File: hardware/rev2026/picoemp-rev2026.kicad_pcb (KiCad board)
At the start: 2 copper layers, 40 x 130 mm, 53 parts, among them J1 EDGE-SMA, J2 1x2_Pin_Header, J3 MKDS 1,5/2-5.08, J4 EDGE-SMA, P1 Header 7, P2 Header 2, P3 Header 4, Q1 LDA111STR, Q2 RGT16BM65DTL, Q3 AO3422, Q4 AO3422, SW1 KSC741J LFS, SW2 KSC741J LFS, SW3 TL3301AF160QJ, T1 ATB322524, T2 ATB322524, U1 SC0915, U2 74LVC1G17

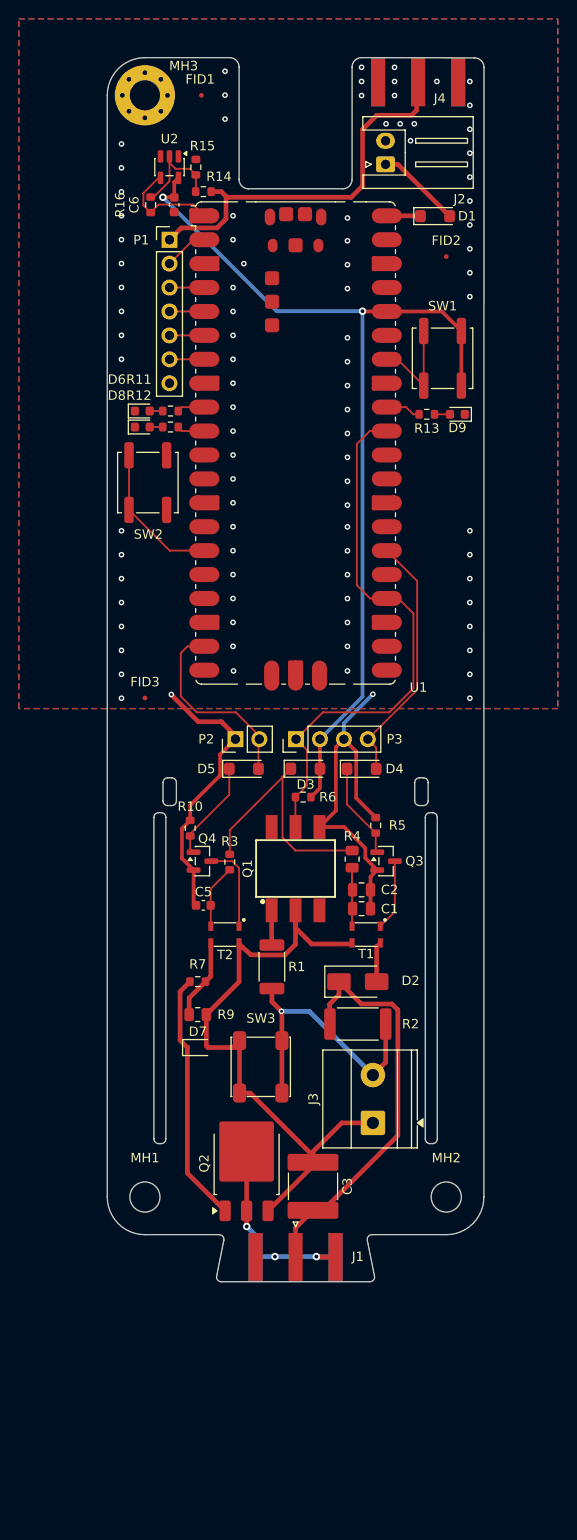
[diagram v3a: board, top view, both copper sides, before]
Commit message: Checkpoint: board origin shift, HV warning marks, intra-HV rule
Committing work that had been sitting uncommitted in the working tree, so the
1551G shield changes can be replayed on top of it without risking it.

  - whole board translated +25.400 mm in Y (X unchanged); origin was 19.872,
    now 45.272
  - two Symbol_HighVoltage_NoTriangle_2x5mm_Copper marks added at the board
    edges beside the HV section, (106.900,139.300) and (141.900,139.300),
    both carrying the unannotated reference REF**
  - .dru gains "Intra-HV spacing at full rail voltage": 0.8 mm, warning
    severity, scoped to the three pairs that genuinely stand at the rail --
    HV_RTN against HV_SENSE, HV_RAIL and HV_OUT. The barrier rule is
    HV-to-non-HV and says nothing about these.
  - schematic: 3 wires, 3 junctions and some repositioning; no component,
    value or property changes
  - LAYOUT-HANDOFF.md rewritten from instructions into a record

Gates at this commit: 66 tests pass; DRC with errors and warnings reports 0
violations, 0 unconnected, 0 footprint errors, exit 0. The new rule fires
correctly and finds nothing -- the header comment claiming 9 violations
predates the fixes that cleared them.

Co-Authored-By: Claude Opus 5 <noreply@anthropic.com>
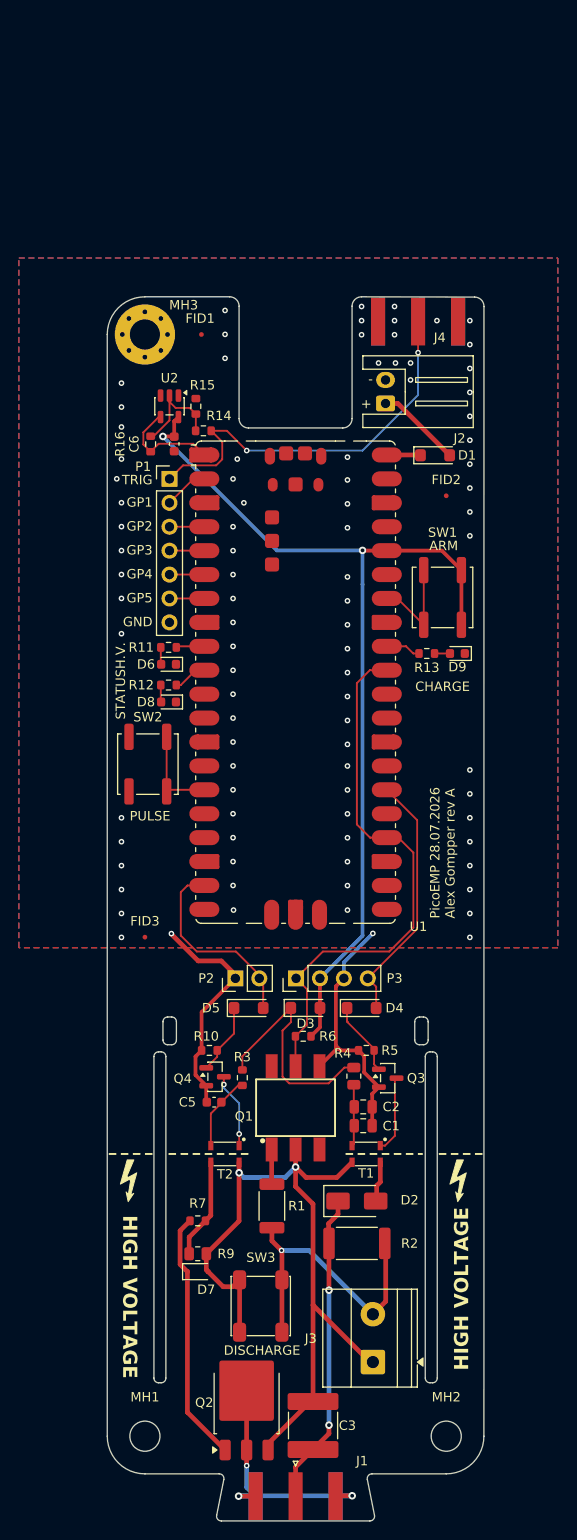
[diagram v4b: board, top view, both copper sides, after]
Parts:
- added REF**: Symbol_HighVoltage_NoTriangle_2x5mm_Copper, Symbol:Symbol_HighVoltage_NoTriangle_2x5mm_Copper, F.Cu at (106.9, 139.3)
- added REF**: Symbol_HighVoltage_NoTriangle_2x5mm_Copper, Symbol:Symbol_HighVoltage_NoTriangle_2x5mm_Copper, F.Cu at (141.9, 139.3)
- moved SW2 29.9 mm to (108.7, 94.9), turned to -90 degrees
- moved D8 29.3 mm to (110.9, 88.3), turned to 180 degrees
- moved R12 27.4 mm to (110.9, 86.5)
- moved D6 27.0 mm to (110.9, 84.3), turned to 180 degrees
- moved D5 25.4 mm to (119.4, 120.8)
- moved D3 25.4 mm to (125.4, 120.8)
- moved D9 25.4 mm to (141.6, 83.2)
- moved FID2 25.4 mm to (140.4, 66.4)
- moved FID3 25.4 mm to (108.4, 113.3)
- moved J3 25.4 mm to (132.6, 158.4)
- moved P2 25.4 mm to (118.0, 117.7)
- moved P3 25.4 mm to (124.4, 117.7)
- moved Q1 25.4 mm to (124.4, 131.4)
- moved R1 25.4 mm to (121.9, 141.8)
- moved R13 25.4 mm to (138.3, 83.2)
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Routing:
- net GND: track 69.1 -> 52.8 mm, vias 91 -> 90
- net /HV_RTN: track 66.6 -> 80.5 mm, vias 0 -> 2
- net /HV_RAIL: track 42.7 -> 33.2 mm, vias 0 -> 2
- net /HV_OUT: track 22.2 -> 31.4 mm
- net /PULSE_SW: track 15.6 -> 9.87 mm
- net /Q4_GATE: track 10.7 -> 7.57 mm
- net /PRI_CLAMP: track 27.4 -> 25.0 mm
- net /Q3_GATE: track 10.2 -> 7.90 mm
- net /HV_GATE_DRV: track 8.44 -> 10.7 mm
- net /HV_SENSE: track 30.9 -> 33.1 mm
- net /T2_PRI_A: track 9.65 -> 7.99 mm, vias 0 -> 2
- net /T1_PRI_B: track 8.02 -> 6.54 mm
- net /TRIG_IN: track 41.7 -> 43.1 mm, vias 0 -> 2
- net /T2_PRI_B: track 6.84 -> 8.04 mm
- net /STATUS_LED: track 2.94 -> 3.63 mm
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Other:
- board text added: "ARM"
- board text added: "CHARGE"
- board text added: "DISCHARGE"
- board text added: "H.V."
- board text added: "HIGH VOLTAGE"
- board text added: "PULSE"
- board text added: "PicoEMP 28.07.2026 Alex Gompper rev A"
- board text added: "STATUS"

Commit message: Drop the 1551B tab slots; mark where the 1551G box lands
Replays the mechanical half of the shield work onto this geometry (+25.400 mm
in Y relative to the branch it was developed on).

The two short Edge.Cuts slots at y 121.754-124.700 were the 1551B half-shell's
snap-tab pockets. With the 1551G box they have no function -- nearest
HV-netclass copper is 16.6 mm, so they were never creepage features either.

Silk now marks the box footprint: 4.5 mm corner brackets at the two NORTH
corners, (106.890,120.272) and (141.890,120.272), plus a "1551G" label. Only
the north corners are marked because the box's south edge is flush with the
board's south body edge and its width is centred -- the north edge is the only
ambiguous dimension. A full witness rectangle was tried first and produced 25
silk violations against the HIGH VOLTAGE legend, the HV warning marks and the
D3/D4/D5 designators; corner brackets clear all of it.

MH1 and MH2 are NOT moved here. The 1551G screws want (112.640,126.022) and
(136.140,164.522) on this geometry. MH2's spot is clear (+1.054 mm). MH1's is
not: GND tracks sit 0.677 mm inside the hole and R10 pad 1 sits 0.206 mm
inside. The fix used on the branch cannot be transplanted -- this layout has
moved 21 footprints including T1, T2, Q3, Q4, C1, C2, C5 and R2-R5, and roughly
150 tracks differ per side, so the surrounding copper is not the same board.

DRC with errors and warnings: 0 violations, 0 unconnected, 0 footprint errors,
exit 0. 66 tests pass.

Co-Authored-By: Claude Opus 5 <noreply@anthropic.com>
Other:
- outline, holes or cut-outs redrawn
- board text added: "1551G"

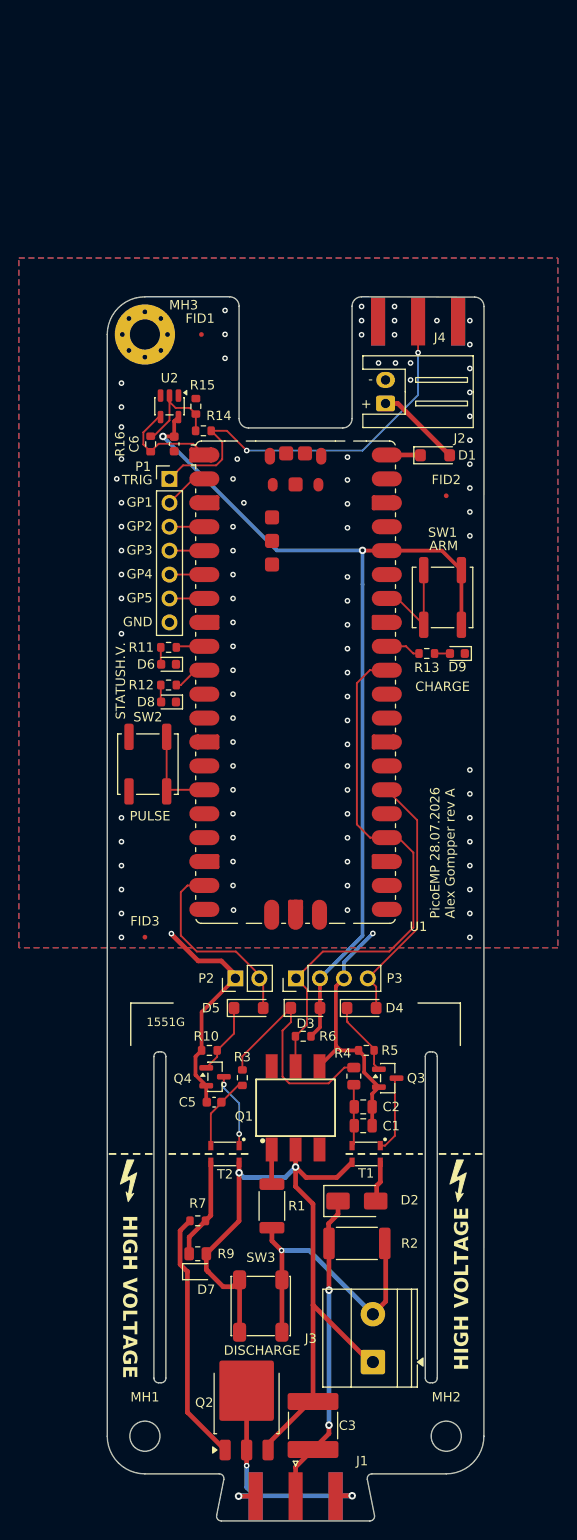
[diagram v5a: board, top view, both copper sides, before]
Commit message: Restore the board carrying the 1551G mounting holes
I merged only two of the three commits off the shield branch and left c8ee8bb --
the mounting holes and Alex's hand reroute of R10 -- stranded. That was the
missing work.

git could not merge the two board files: they are different boards, one being
the other translated +25.400 mm in Y with 21 footprints moved and ~150 tracks
different per side, so a textual merge produces nothing meaningful. Taking
c8ee8bb's board wholesale instead.

This board has:
  MH1 (112.640,100.622) and MH2 (136.140,139.122) -- the 1551G's diagonal
      screw axes, so the box can actually be screwed down
  R10 (116.900,103.400) rot 180 with GND jogged to B.Cu past the hole
  the two 1551B snap-tab slots removed
  a silk witness outline for the box

The other board -- the +25.400 mm re-layout with the HV warning marks -- is
preserved on branch relayout-shifted-25mm and in history at 236e65b. Nothing is
lost either way; swapping back is one checkout.

Gates: 66 tests pass. DRC --severity-error: 0 violations, 0 unconnected,
0 parity issues, exit 0. One warning remains, the intra-HV rule reporting
0.648 mm against its 0.8 mm target between the HV_RTN track and C3 pad 2 --
IPC-2221A B1 requires 0.40 mm at 171-300 V, so it is compliant; the rule is a
deliberately tighter goal at warning severity. That rule came in with the other
line and had never been applied to this board.

CLAUDE.md and LAYOUT-HANDOFF.md still quote the shifted coordinates and counts.
Correcting next.

Co-Authored-By: Claude Opus 5 <noreply@anthropic.com>
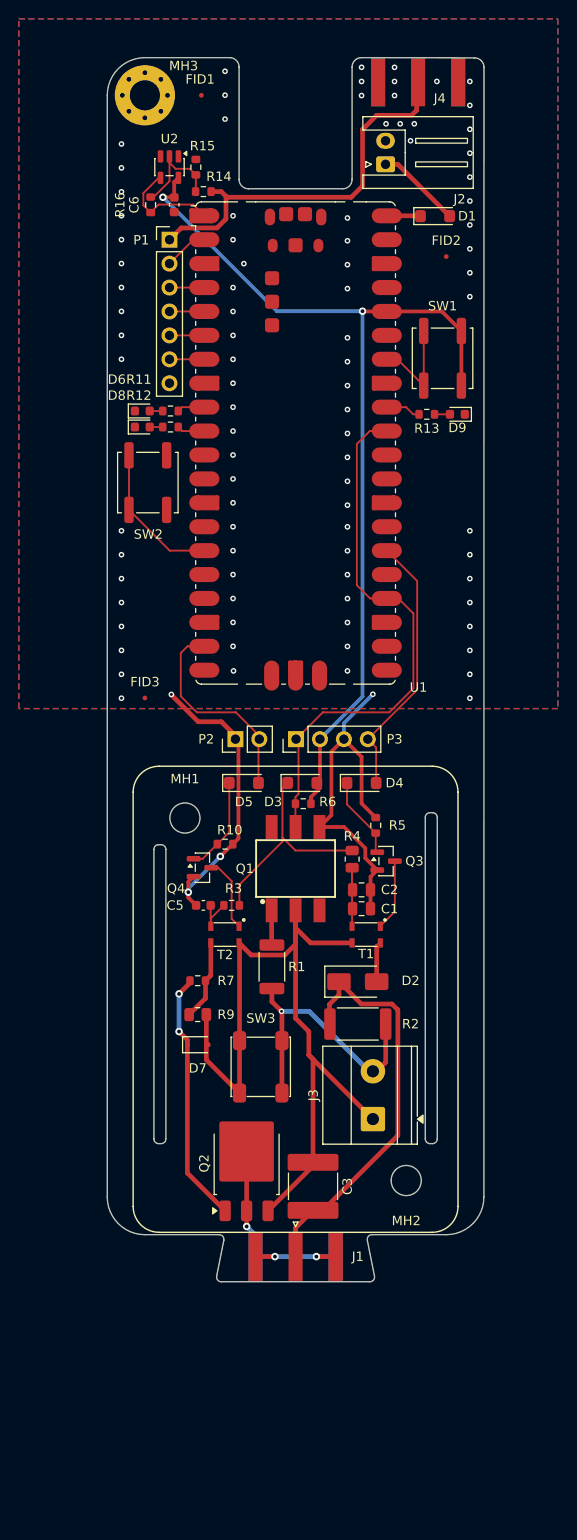
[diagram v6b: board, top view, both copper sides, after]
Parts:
- removed REF** (x2): Symbol_HighVoltage_NoTriangle_2x5mm_Copper, Symbol:Symbol_HighVoltage_NoTriangle_2x5mm_Copper
- moved MH1 65.8 mm to (112.6, 100.6)
- moved SW2 29.9 mm to (108.7, 65.0), turned to 90 degrees
- moved D8 29.3 mm to (108.1, 59.1), turned to 0 degrees
- moved MH2 27.5 mm to (136.1, 139.1)
- moved R12 27.4 mm to (111.1, 59.1)
- moved D6 27.0 mm to (108.1, 57.4), turned to 0 degrees
- moved J3 25.8 mm to (132.6, 132.6)
- moved R7 25.5 mm to (114.0, 117.9)
- moved D9 25.4 mm to (141.6, 57.8)
- moved FID2 25.4 mm to (140.4, 41.0)
- moved FID3 25.4 mm to (108.4, 87.9)
- moved P2 25.4 mm to (118.0, 92.2)
- moved P3 25.4 mm to (124.4, 92.2)
- moved Q1 25.4 mm to (124.4, 106.0)
- moved R1 25.4 mm to (121.9, 116.4)
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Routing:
- net GND: track 52.8 -> 70.6 mm, vias 90 -> 93
- net /HV_RAIL: track 33.2 -> 42.7 mm, vias 2 -> 0
- net /HV_RTN: track 80.5 -> 89.2 mm, vias 2 -> 0
- net /HV_OUT: track 31.4 -> 24.3 mm
- net /PULSE_SW: track 9.87 -> 15.6 mm
- net /T2_PRI_B: track 8.04 -> 4.19 mm
- net /Q4_GATE: track 7.57 -> 10.2 mm
- net /HV_SENSE: track 33.1 -> 30.8 mm
- net /HV_GATE_DRV: track 10.7 -> 8.57 mm
- net /PRI_CLAMP: track 25.0 -> 23.1 mm
- net /HVPWM: track 27.0 -> 28.5 mm
- net /T1_PRI_B: track 6.54 -> 8.02 mm
- net /TRIG_IN: track 43.1 -> 41.7 mm, vias 2 -> 0
- net /HVPULSE: track 21.4 -> 22.7 mm
- net +3V3: track 100.7 -> 101.7 mm
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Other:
- outline, holes or cut-outs redrawn
- board text removed: "1551G"
- board text removed: "ARM"
- board text removed: "CHARGE"
- board text removed: "DISCHARGE"
- board text removed: "H.V."
- board text removed: "HIGH VOLTAGE"
- board text removed: "PULSE"
- board text removed: "PicoEMP 28.07.2026 Alex Gompper rev A"
- board text removed: "STATUS"

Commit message: Move D3/D4/D5 clear of the shield rim; close the intra-HV gap
Alex's interactive work in pcbnew.

  D3 (125.100,96.900) -> (124.800,98.400)
  D4 (131.400,96.900) -> (131.350,98.400)
  D5 (118.900,96.900) -> (118.850,98.400)

That is the +1.5 mm south the isolation diodes needed to clear the 1551G's rim
contact band. R6 moved out of D3's way, (125.200,99.100) -> (128.100,98.075)
rot 90. Q1, Q4 and SW2 nudged with them, and about 50 track segments rerouted
across GND, Q4_GATE, T2_PRI_A and PULSE_SW.

The intra-HV warning is gone too: the rule's 0.8 mm target now passes, where it
was reporting 0.648 mm between the HV_RTN track and C3 pad 2.

Gates: 66 tests pass; DRC --severity-error exit 0; DRC including warnings also
reports 0 violations, 0 unconnected, 0 footprint errors; ERC exit 0.

Co-Authored-By: Claude Opus 5 <noreply@anthropic.com>
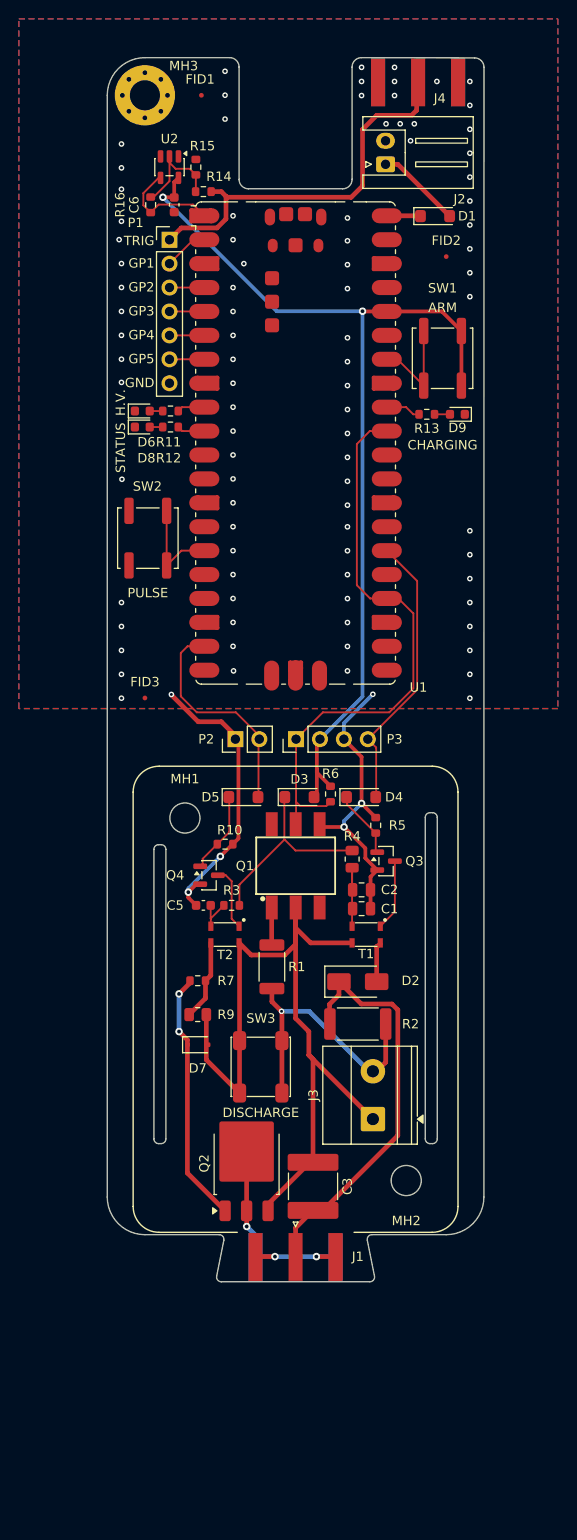
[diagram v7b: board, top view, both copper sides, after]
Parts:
- moved SW2 5.90 mm to (108.7, 70.9), turned to -90 degrees
- moved R6 3.08 mm to (128.1, 98.1), turned to 90 degrees
- moved D3 1.53 mm to (124.8, 98.4)
- moved D4 1.50 mm to (131.3, 98.4)
- moved D5 1.50 mm to (118.8, 98.4)
- moved Q4 1.06 mm to (115.2, 106.7)
- moved Q1 0.30 mm to (124.4, 105.7)
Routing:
- net GND: track 70.6 -> 63.6 mm, vias 93 -> 94
- net /PULSE_SW: track 15.6 -> 10.5 mm
- net /CHARGED: track 58.2 -> 61.7 mm
- net /PRI_CLAMP: track 23.1 -> 21.1 mm
- net /Q4_GATE: track 10.2 -> 8.65 mm
- net /HVPULSE: track 22.7 -> 24.2 mm
- net /HVPWM: track 28.5 -> 30.1 mm
- net /Q3_GATE: track 8.68 -> 7.20 mm
- net +3V3: track 101.7 -> 102.9 mm
- net /HV_RTN: track 89.2 -> 90.3 mm
- net /T2_PRI_A: track 7.87 -> 6.84 mm
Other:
- board text added: "ARM"
- board text added: "CHARGING"
- board text added: "DISCHARGE"
- board text added: "H.V."
- board text added: "PULSE"
- board text added: "STATUS"

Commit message: Q2 clear of the shield rim; board re-shifted +25.400 mm; silkscreen added
Alex's work, committed as-is ahead of ordering.

  every footprint translated +25.400 mm in Y, except Q2, which moved +24.300 --
  i.e. 1.100 mm north of the shift. That is the Q2 fix: it was the last part
  fouling the 1551G rim, needing ~0.4 mm with 0.6 for margin.
  MH1 (112.640,126.022) and MH2 (136.140,164.522) -- still exactly on the
  1551G's diagonal screw axes after the shift.
  4 more board-level silkscreen objects, 1 more track.

Gates: 66 tests pass; DRC --severity-error exit 0 with 0 violations and
0 unconnected; ERC exit 0.

With warnings included there are now 3 footprint_symbol_mismatch warnings --
FID1, FID2 and FID3 disagree with their symbols on the 'Do not populate' flag.
Left alone deliberately. Fiducials are copper features, so this changes nothing
in the gerbers; it only affects whether they land in a placement file. Worth
reconciling before generating CPL output, not before ordering bare boards.

Co-Authored-By: Claude Opus 5 <noreply@anthropic.com>
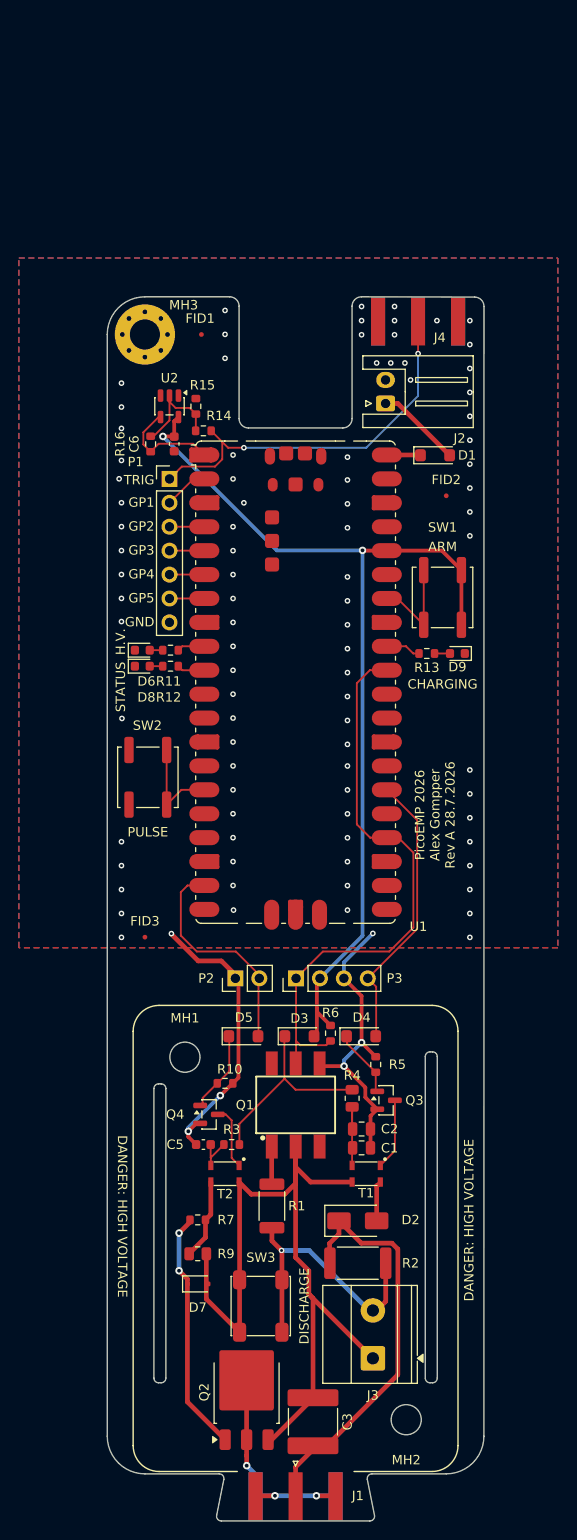
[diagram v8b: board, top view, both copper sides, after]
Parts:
- moved C1 25.4 mm to (131.4, 135.7)
- moved C2 25.4 mm to (131.4, 133.7)
- moved C5 25.4 mm to (114.6, 135.3)
- moved D2 25.4 mm to (131.0, 143.4)
- moved D9 25.4 mm to (141.6, 83.2)
- moved FID2 25.4 mm to (140.4, 66.4)
- moved FID3 25.4 mm to (108.4, 113.3)
- moved J3 25.4 mm to (132.6, 158.0)
- moved MH1 25.4 mm to (112.6, 126.0)
- moved P2 25.4 mm to (118.0, 117.7)
- moved P3 25.4 mm to (124.4, 117.7)
- moved R1 25.4 mm to (121.9, 141.8)
- moved R10 25.4 mm to (116.9, 128.8)
- moved R13 25.4 mm to (138.3, 83.2)
- moved R2 25.4 mm to (131.0, 147.9)
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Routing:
- net /HV_GATE: track 26.9 -> 25.8 mm
- net /HV_OUT: track 24.3 -> 25.4 mm
- net /HV_RTN: track 90.3 -> 89.2 mm
- net /TRIG_IN: track 41.7 -> 41.2 mm, vias 0 -> 2
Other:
- board text added: "DANGER: HIGH VOLTAGE"
- board text added: "PicoEMP 2026 Alex Gompper Rev A 28.7.2026"
